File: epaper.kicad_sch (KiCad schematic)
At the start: 18 parts, among them J6 E-Paper, Q2 AP2302B

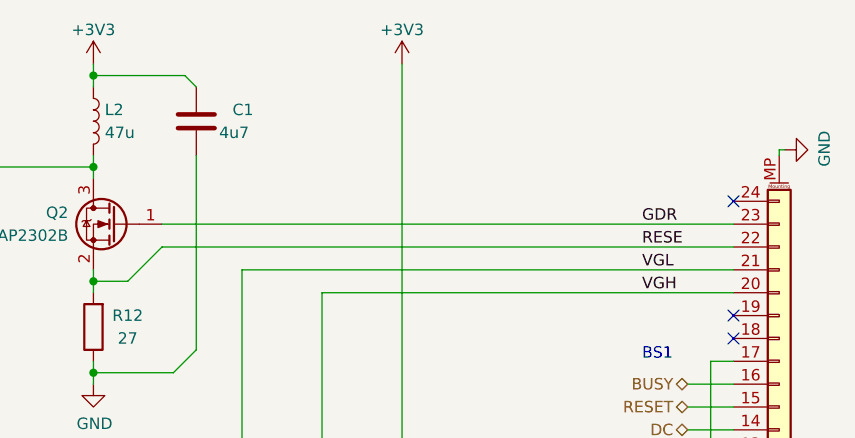
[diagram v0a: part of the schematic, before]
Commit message: V1.1 almost complete update
✔️add a 100k resistor between the gate of the FET in the epaper circuit and ground
✔️Moved LEDs to match the alignment on line “HIKL” and “Y”
✔️Change polarity on the LEDs, they are the “wrong way around” (software thing only, doesn’t matter for charlieplexing
-Add relay control on PD7 (if it can be changed)
✔️Swap PA1 and PA2 with PD3 and PD2
✔️ Prog pads for CH32
✔️Connect SAO IOs to relay output (to make an add-on glow when the relay ticks), pulled low by default.
✔️ Move relay
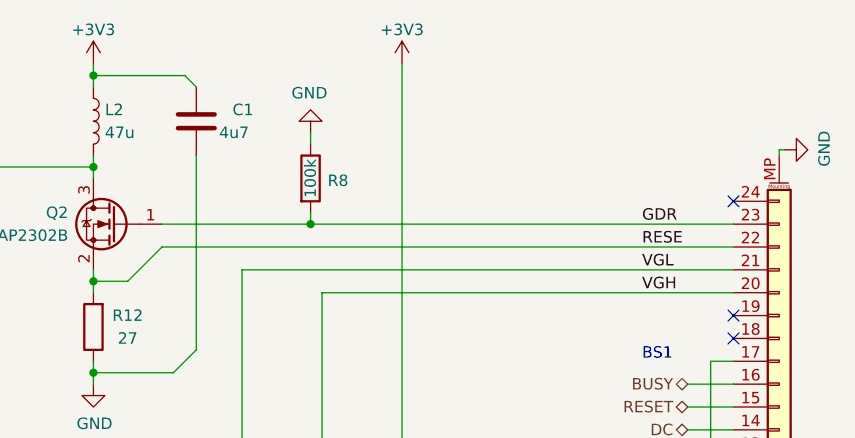
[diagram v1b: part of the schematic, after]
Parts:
- added R8: 100k, Resistor_SMD:R_0805_2012Metric, symbol symbols:R
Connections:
- net GDR: now also R8.2
- net GND: now also R8.1
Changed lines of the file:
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@@
   (junction (at 87.63 130.81) (diameter 0) (color 0 0 0 0)
+  )
+  (junction (at 130.81 60.96) (diameter 0) (color 0 0 0 0)
   )
   (junction (at 95.25 130.81) (diameter 0) (color 0 0 0 0)
@@
     (stroke (width 0) (type default))
   )
+  (wire (pts (xy 130.81 60.96) (xy 130.81 59.69))
+    (stroke (width 0) (type default))
+  )
   (wire (pts (xy 146.05 101.6) (xy 177.8 101.6))
     (stroke (width 0) (type default))
@@
     (stroke (width 0) (type default))
   )
-  (wire (pts (xy 114.3 60.96) (xy 177.8 60.96))
+  (wire (pts (xy 114.3 60.96) (xy 130.81 60.96))
     (stroke (width 0) (type default))
   )
@@
     (stroke (width 0) (type default))
   )
+  (wire (pts (xy 130.81 60.96) (xy 177.8 60.96))
+    (stroke (width 0) (type default))
+  )
   (wire (pts (xy 140.97 96.52) (xy 177.8 96.52))
     (stroke (width 0) (type default))
@@
   )
   (wire (pts (xy 95.25 128.27) (xy 95.25 130.81))
+    (stroke (width 0) (type default))
+  )
+  (wire (pts (xy 130.81 52.07) (xy 130.81 50.8))
     (stroke (width 0) (type default))
   )
@@
     )
   )
+  (symbol (lib_id "symbols:R") (at 130.81 55.88 0) (unit 1)
+    (exclude_from_sim no) (in_bom yes) (on_board yes) (dnp no)
+    (property "Reference" "R8" (at 133.858 56.134 0)
+      (effects (font (size 1.27 1.27)))
+    )
+    (property "Value" "100k" (at 130.81 55.88 90)
+      (effects (font (size 1.27 1.27)))
+    )
+    (property "Footprint" "Resistor_SMD:R_0805_2012Metric" (at 129.032 55.88 90)
+      (effects (font (size 1.27 1.27)) hide)
+    )
+    (property "Datasheet" "https://datasheet.lcsc.com/lcsc/2308241947_FOJAN-FRC0805J104-TS_C2907293.pdf" (at 130.81 55.88 0)
+      (effects (font (size 1.27 1.27)) hide)
+    )
+    (property "Description" "" (at 130.81 55.88 0)
+      (effects (font (size 1.27 1.27)) hide)
+    )
+    (property "LCSC" "C2907293" (at 130.81 55.88 0)
+      (effects (font (size 1.27 1.27)) hide)
+    )
+    (property "Buy early" "" (at 130.81 55.88 0)
+      (effects (font (size 1.27 1.27)) hide)
+    )
+    (property "Category" "" (at 130.81 55.88 0)
+      (effects (font (size 1.27 1.27)) hide)
+    )
+    (property "MANUFACTURER" "" (at 130.81 55.88 0)
+      (effects (font (size 1.27 1.27)) hide)
+    )
+    (property "MPN" "" (at 130.81 55.88 0)
+      (effects (font (size 1.27 1.27)) hide)
+    )
+    (property "Manufacturer" "" (at 130.81 55.88 0)
+      (effects (font (size 1.27 1.27)) hide)
+    )
+    (property "Mouser" "" (at 130.81 55.88 0)
+      (effects (font (size 1.27 1.27)) hide)
+    )
+    (property "Price" "" (at 130.81 55.88 0)
+      (effects (font (size 1.27 1.27)) hide)
+    )
+    (property "Quantity" "" (at 130.81 55.88 0)
+      (effects (font (size 1.27 1.27)) hide)
+    )
+    (property "Sponsored" "" (at 130.81 55.88 0)
+      (effects (font (size 1.27 1.27)) hide)
+    )
+    (property "Field-1" "" (at 130.81 55.88 0)
+      (effects (font (size 1.27 1.27)) hide)
+    )
+    (property "Link" "https://www.lcsc.com/product-detail/Chip-span-style-background-color-ff0-Resistor-span-Surface-Mount_FOJAN-FRC0805J104-TS_C2907293.html" (at 130.81 55.88 0)
+      (effects (font (size 1.27 1.27)) hide)
+    )
+    (pin "1")
+    (pin "2")
+    (instances
+      (project "hh2024"
+        (path "/5f312b85-6822-40a3-b417-2df49696ca2d"
+          (reference "R8") (unit 1)
+        )
+        (path "/5f312b85-6822-40a3-b417-2df49696ca2d/77fdc604-e080-44e7-9e66-e31abda69ba3"
+          (reference "R31") (unit 1)
+        )
+        (path "/5f312b85-6822-40a3-b417-2df49696ca2d/167dea4c-c9e2-4e60-aa6f-1e8f992a867c"
+          (reference "R36") (unit 1)
+        )
+      )
+    )
+  )
   (symbol (lib_id "symbols:C") (at 132.08 128.27 180) (unit 1)
     (exclude_from_sim no) (in_bom yes) (on_board yes) (dnp no)
@@
         )
       )
+    )
+  )
+  (symbol (lib_id "symbols2:GND") (at 130.81 50.8 180) (unit 1)
+    (exclude_from_sim no) (in_bom yes) (on_board yes) (dnp no)
+    (property "Reference" "#PWR0131" (at 130.81 44.45 0)
+      (effects (font (size 1.27 1.27)) hide)
+    )
+    (property "Value" "GND" (at 130.683 46.4058 0)
+      (effects (font (size 1.27 1.27)))
+    )
+    (property "Footprint" "" (at 130.81 50.8 0)
+      (effects (font (size 1.27 1.27)) hide)
+    )
+    (property "Datasheet" "" (at 130.81 50.8 0)
+      (effects (font (size 1.27 1.27)) hide)
+    )
+    (property "Description" "Power symbol creates a global label with name \"GND\" , ground" (at 130.81 50.8 0)
+      (effects (font (size 1.27 1.27)) hide)
+    )
+    (pin "1")
+    (instances
+      (project "hh2024"
+        (path "/5f312b85-6822-40a3-b417-2df49696ca2d"
+          (reference "#PWR0131") (unit 1)
+        )
+        (path "/5f312b85-6822-40a3-b417-2df49696ca2d/77fdc604-e080-44e7-9e66-e31abda69ba3"
+          (reference "#PWR050") (unit 1)
+        )
+        (path "/5f312b85-6822-40a3-b417-2df49696ca2d/167dea4c-c9e2-4e60-aa6f-1e8f992a867c"
+          (reference "#PWR018") (unit 1)
+        )
+      )

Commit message: V1.2
added reverse mount RGB LED
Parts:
- R12: now in the parts list
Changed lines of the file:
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@@
   )
   (symbol (lib_id "symbols:R") (at 140.97 100.33 0) (unit 1)
-    (exclude_from_sim no) (in_bom no) (on_board yes) (dnp yes)
+    (exclude_from_sim no) (in_bom yes) (on_board yes) (dnp yes)
     (property "Reference" "R12" (at 137.16 99.06 0)
       (effects (font (size 1.27 1.27)))

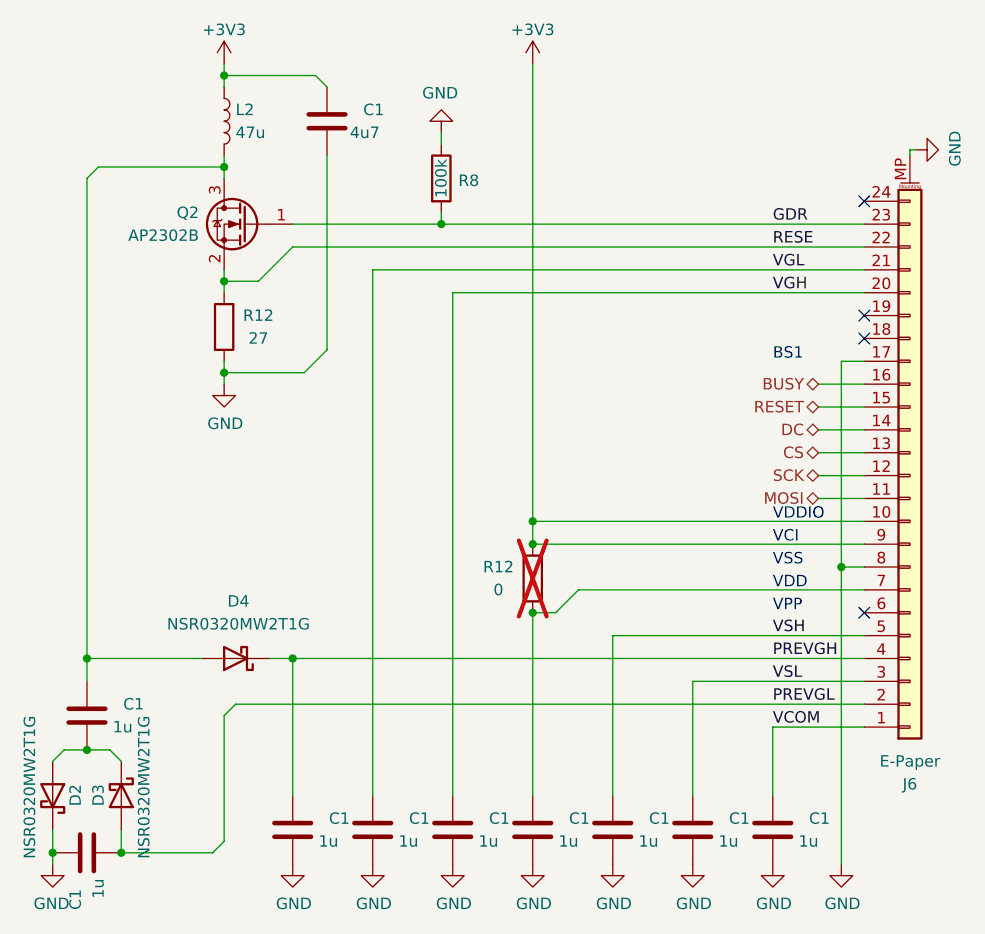
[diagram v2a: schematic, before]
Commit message: V1.3
Changed C23 from 1uF to 0.47uF
Changed R21 from 27ohms to 2.2ohms
Changed C17 from 4.7uF to 1uF
Removed R37 and R38, R39 and R40
Added J2 QWIIC connector
Added U6 buffer to drive SK6085 LED
Removed R33 to a direct wire connection
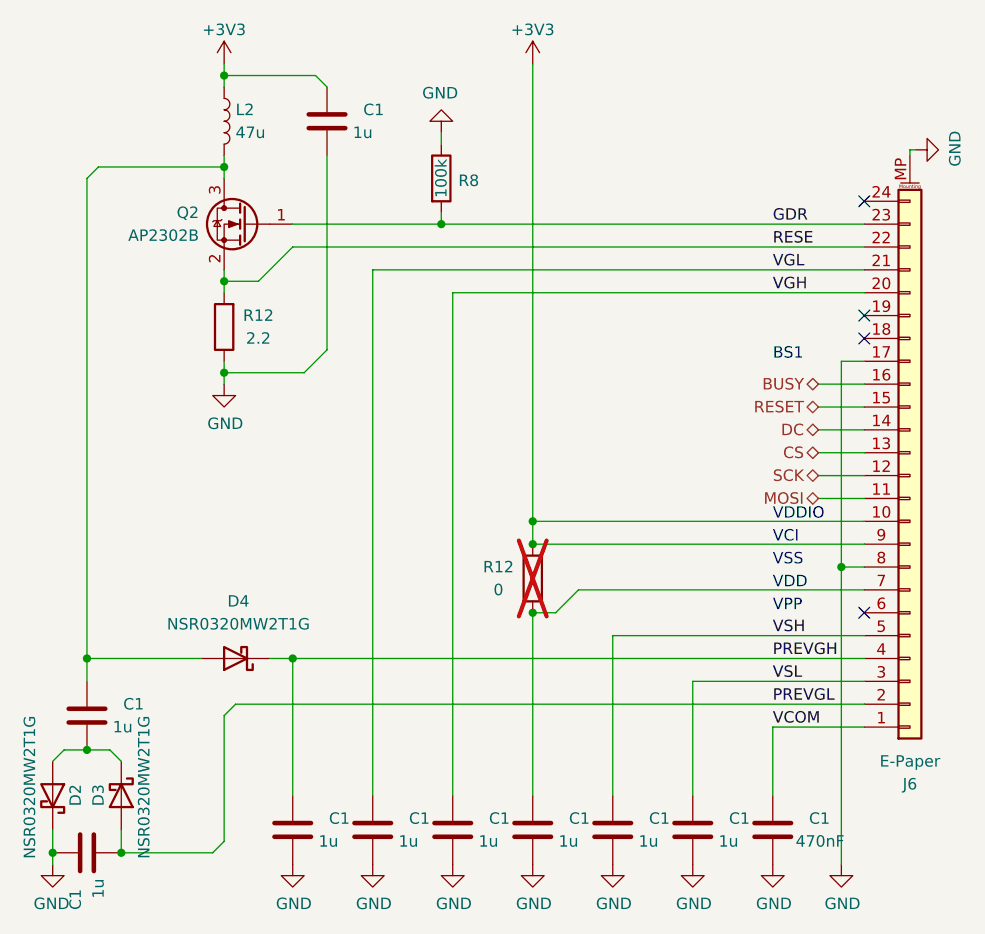
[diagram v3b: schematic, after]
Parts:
- C1: value 4u7 -> 470nF; LCSC C2918489 -> C2859120; Link https://www.lcsc.com/product-detail/Multilayer-Ceramic-Capacitors-MLCC-SMD-SMT_Samwha-Capacitor-CS2012X5R475K250NRE_C2918489.html -> https://www.lcsc.com/product-detail/Multilayer-Ceramic-Capacitors-MLCC-SMD-SMT_FH-Guangdong-Fenghua-Advanced-Tech-0805B474K250NT_C2859120.html
- R12: value 27 -> 2.2; LCSC C2907314 -> C2907304; Link https://www.lcsc.com/product-detail/Chip-span-style-backgro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 -> https://www.lcsc.com/product-detail/Chip-Resistor-Surface-M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
- R12: now left out of the parts list
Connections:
- net +3V3: now also C1.2; no longer C1.2
- net VCOM: now also C1.2; no longer C1.2
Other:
- moved on the sheet: C1

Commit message: Small fixes and change footprint library for missing libraries
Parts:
- C17: renamed from C1; value 1u -> 4.7u; LCSC C376929 -> (none); Link https://www.lcsc.com/product-detail/Multilayer-Ceramic-Capa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 -> (none)
- C23: renamed from C1; value 470nF -> 470n
- D2, D3, D4: footprint tanoshii:D_SOD-323 -> hh24:D_SOD-323
- J6: footprint tanoshii:Hirose_FH12-24S-0.5SH_1x24-1MP_P0.50mm_Horizontal -> hh24:Hirose_FH12-24S-0.5SH_1x24-1MP_P0.50mm_Horizontal
- L2: footprint tanoshii:L_1210_3225Metric -> hh24:L_1210_3225Metric
- Q2: footprint tanoshii:SOT-23 -> hh24:SOT-23
- renumbered C1 to C14, C1 to C15, C1 to C16, C1 to C18, C1 to C19, C1 to C20, C1 to C21, C1 to C22, R12 to R21, R12 to R22, R8 to R36
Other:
- company: Nicolai Electronics -> Nicolai Electronics & tilde.industries
- moved on the sheet: C17, R36

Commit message: Moar headers
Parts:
- renumbered C14 to C13, C15 to C14, C17 to C15, C18 to C17, C19 to C18, C20 to C19, C21 to C20, C22 to C21, C23 to C22, D2 to D25, D3 to D26, D4 to D27, J6 to J10, Q2 to Q3, R21 to R34, R36 to R35, R22 to R36

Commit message: tidy silk and solved DRC errors
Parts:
- C15: LCSC (none) -> C2918489; Link (none) -> https://www.lcsc.com/product-detail/Multilayer-Ceramic-Capa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
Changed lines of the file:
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@@
 			)
 		)
-		(property "Datasheet" ""
+		(property "Datasheet" "https://datasheet.lcsc.com/lcsc/2111172030_Samwha-Capacitor-CS2012X5R475K250NRE_C2918489.pdf"
 			(at 96.52 72.39 0)
 			(effects
@@
 			)
 		)
-		(property "LCSC" ""
+		(property "LCSC" "C2918489"
 			(at 96.52 72.39 0)
 			(effects
@@
 			)
 		)
-		(property "Link" ""
+		(property "Link" "https://www.lcsc.com/product-detail/Multilayer-Ceramic-Capacitors-MLCC-SMD-SMT_Samwha-Capacitor-CS2012X5R475K250NRE_C2918489.html"
 			(at 96.52 72.39 0)
 			(effects
